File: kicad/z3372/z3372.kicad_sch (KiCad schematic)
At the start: 34 parts, among them J1 Conn_01x01, J2 Conn_01x02, J3 Conn_02x20_Odd_Even, Q4 MMBT3904, U1 MUX508, U15 M24C02-WMN, U2 MUX508, U3 TL074, U7 CAT9555YI-T2

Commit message: checkpoint z3372 v0.4
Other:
- sheet DAC ports: added FINAL_VCA4_CV; removed none
- sheet filter_as3372 ports: added VCA4_CV; removed none
- note added: "GPIO Module Driven: This mess is intended to be a peak voltage detector with a short hold cap. Trigger a +5V gate for the GPIO Module Driven signal. This can be used to crudely calibrate the noise level or resonance."
- note removed: "GPIO Module Driven: This mess is intended to be a peak voltage detector with a hold cap that doesn't hold all that long. Trigger a +5V gate for the GPIO Module Driven signal. This can be used to crudely calibrate the noise level or resonance."
- title: Z3372 Signal Processing -> Z3372 Signal Processor

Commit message: schematic done.  some values need tweaking.  design review still needed
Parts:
- removed unit 3 of U3
- added C29: 1u, Capacitor_SMD:C_0603_1608Metric, symbol Device:C
- added R35: 4k7, Resistor_SMD:R_1206_3216Metric, symbol Device:R
- added U5: LM4040AIM3-2.5, Package_TO_SOT_SMD:SOT-23, symbol Reference_Voltage:LM4040DBZ-2.5
- U1, U2: symbol as3372_lib:PS508-Analog_Switch -> z3372_lib:PS508-Analog_Switch
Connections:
- net +5V: now also R35.1
- net GND: now also C29.2, U5.2 (A)
- net PAN_FM_CTRL: now reaches U7.9 (IO0_5)
- net WHITE_NOISE_CTRL: no longer names the net of U7.10 (IO0_6)
- new net VREF_2.5V: C29.1, R35.2, U5.1 (K)
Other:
- sheet DAC ports: added MOD_AMOUNT_CV, VREF_2.5; removed MOD_AMOUNT_VCA3_CV
- sheet filter_as3372 ports: added PAN_FM_CTRL, VREF_2.5; removed NOISE_CTRL
- note added: "LM4040 resistor rough calc: Ilm4040 min: 70uA Vref input impedance: 3k8"
- note added: "TODO: this is likely ~3k"
- note removed: "Spares"
- moved on the sheet: C1, C2, C21, C3, C4, C5, C6, D1, Q4, R1, R17, R2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

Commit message: review underway for AS3372
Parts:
- removed C21: 0.1u, Capacitor_SMD:C_0603_1608Metric, symbol Device:C
- added unit 3 of U3
- R3: value 4k7 -> 100k; LCSC Part C23162 -> (none)
- R35: value 4k7 -> 3k; LCSC Part C17936 -> (none)
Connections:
- net GND: now also U3.10 (+)
- new net: U3.8, U3.9 (-)
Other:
- note added: "LM4040 resistor calc: Vref input impedance total: 3k8 ==> 657 uA lm4040 min: 80uA; with margin shoot for 150uA 657 + 150 ==> 807 uA through R. R = 3097. Use 3k which gives 833 uA."
- note added: "Spares"
- note added: "Voltage Reference"
- note removed: "LM4040 resistor rough calc: Ilm4040 min: 70uA Vref input impedance: 3k8"
- note removed: "TODO: this is likely ~3k"
- moved on the sheet: D4, R3

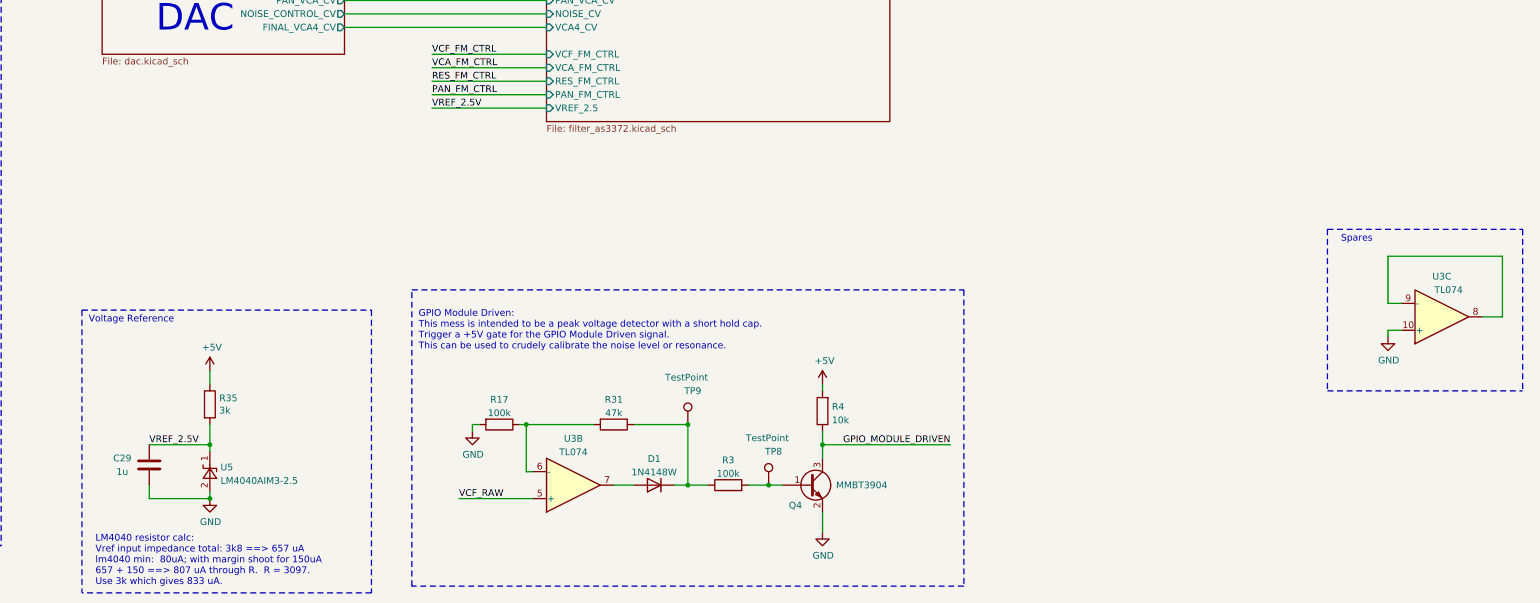
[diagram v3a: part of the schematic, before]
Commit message: schematic completed, working on place and route
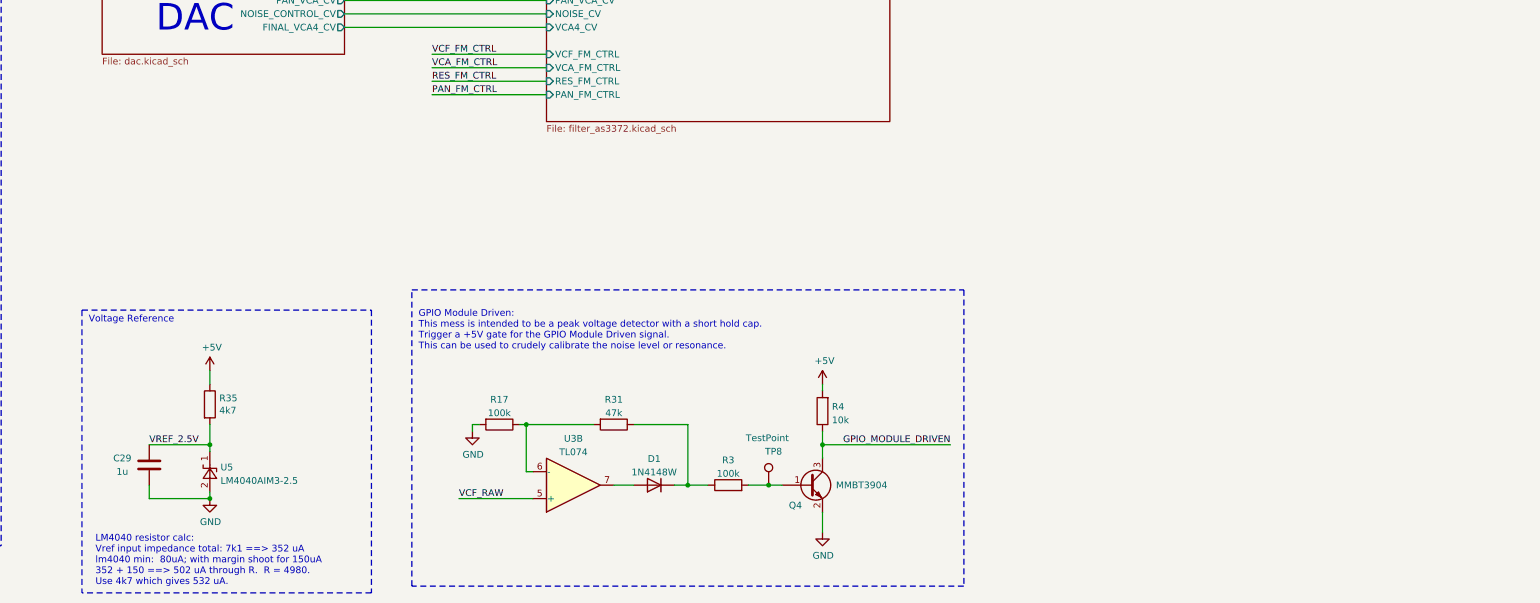
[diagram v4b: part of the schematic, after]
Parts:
- removed TP9: TestPoint, TestPoint:TestPoint_Pad_2.0x2.0mm, symbol Connector:TestPoint
- removed unit 3 of U3
- C29: footprint Capacitor_SMD:C_0603_1608Metric -> Capacitor_SMD:C_0805_2012Metric; LCSC Part (none) -> C28323
- R1, R2: footprint Resistor_SMD:R_0402_1005Metric -> Resistor_SMD:R_0603_1608Metric; LCSC Part C25741 -> C25803
- R3: LCSC Part (none) -> C25803
- R35: value 3k -> 4k7; footprint Resistor_SMD:R_1206_3216Metric -> Resistor_SMD:R_0603_1608Metric; LCSC Part (none) -> C23162
- U3: footprint Package_SO:SOIC-14_3.9x8.7mm_P1.27mm -> Package_SO:TSSOP-14_4.4x5mm_P0.65mm; LCSC Part C12594 -> C96507
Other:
- sheet filter_as3372 ports: added none; removed VREF_2.5
- note added: "LM4040 resistor calc: Vref input impedance total: 7k1 ==> 352 uA lm4040 min: 80uA; with margin shoot for 150uA 352 + 150 ==> 502 uA through R. R = 4980. Use 4k7 which gives 532 uA."
- note removed: "LM4040 resistor calc: Vref input impedance total: 3k8 ==> 657 uA lm4040 min: 80uA; with margin shoot for 150uA 657 + 150 ==> 807 uA through R. R = 3097. Use 3k which gives 833 uA."
- note removed: "Spares"

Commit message: placement improvements
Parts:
- added unit 2 of U3
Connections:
- net GND: now also U3.5 (+)
- net VCF_RAW: now also U3.3 (+); no longer U3.5 (+)
- net VCF_SIGNAL2: now also U3.8, U3.9 (-); no longer U3.1, U3.2 (-)
- net at R2.2, U2.8 (D): now also U3.10 (+); no longer U3.3 (+)
- net at R17.1, R31.2: now also U3.2 (-); no longer U3.6 (-)
- net at D1.2 (A): now also U3.1; no longer U3.7
- new net: U3.6 (-), U3.7
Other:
- note added: "Spares"

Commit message: continue routing
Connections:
- net LED_CTRL: now also U7.4 (IO0_0); no longer U7.6 (IO0_2)
- net RES_FM_CTRL: now also U7.7 (IO0_3); no longer U7.5 (IO0_1)
- net VCF_FM_CTRL: now also U7.6 (IO0_2); no longer U7.4 (IO0_0)
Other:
- moved on the sheet: D4, R56
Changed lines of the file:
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@@
   (no_connect (at 77.47 33.02))
   (no_connect (at 193.04 62.23))
-  (no_connect (at 193.04 52.07))
+  (no_connect (at 193.04 46.99))
   (no_connect (at 64.77 30.48))
   (wire (pts (xy 256.54 245.11) (xy 260.35 245.11))
@@
     (stroke (width 0) (type default))
   )
-  (wire (pts (xy 193.04 46.99) (xy 212.09 46.99))
+  (wire (pts (xy 193.04 52.07) (xy 212.09 52.07))
     (stroke (width 0) (type default))
   )
@@
     (stroke (width 0) (type default))
   )
-  (wire (pts (xy 222.25 46.99) (xy 222.25 49.53))
+  (wire (pts (xy 220.98 41.91) (xy 220.98 44.45))
     (stroke (width 0) (type default))
   )
@@
     (stroke (width 0) (type dash))
   )
-  (wire (pts (xy 193.04 49.53) (xy 214.63 49.53))
-    (stroke (width 0) (type default))
-  )
   (wire (pts (xy 93.98 138.43) (xy 96.52 138.43))
     (stroke (width 0) (type default))
   )
-  (wire (pts (xy 222.25 36.83) (xy 222.25 39.37))
+  (wire (pts (xy 220.98 31.75) (xy 220.98 34.29))
     (stroke (width 0) (type default))
   )
@@
     (stroke (width 0) (type dash))
   )
+  (wire (pts (xy 193.04 54.61) (xy 212.09 54.61))
+    (stroke (width 0) (type default))
+  )
   (wire (pts (xy 104.14 55.88) (xy 104.14 60.96))
     (stroke (width 0) (type default))
@@
     (stroke (width 0) (type default))
   )
-  (wire (pts (xy 193.04 54.61) (xy 212.09 54.61))
-    (stroke (width 0) (type default))
-  )
   (wire (pts (xy 110.49 245.11) (xy 107.95 245.11))
     (stroke (width 0) (type default))
@@
     (stroke (width 0) (type default))
   )
+  (wire (pts (xy 193.04 44.45) (xy 213.36 44.45))
+    (stroke (width 0) (type default))
+  )
   (wire (pts (xy 403.86 208.28) (xy 405.13 208.28))
     (stroke (width 0) (type default))
@@
     (stroke (width 0) (type default))
   )
-  (wire (pts (xy 193.04 44.45) (xy 212.09 44.45))
+  (wire (pts (xy 193.04 49.53) (xy 212.09 49.53))
     (stroke (width 0) (type default))
   )
@@
     (effects (font (size 1.27 1.27)) (justify right bottom))
   )
-  (label "LED_CTRL" (at 199.39 49.53 0) (fields_autoplaced)
-    (effects (font (size 1.27 1.27)) (justify left bottom))
+  (label "LED_CTRL" (at 212.09 44.45 180) (fields_autoplaced)
+    (effects (font (size 1.27 1.27)) (justify right bottom))
   )
   (label "VCF_SIG2_CTRL0" (at 45.72 240.03 270) (fields_autoplaced)
@@
     (effects (font (size 1.27 1.27)) (justify left bottom))
   )
-  (label "RES_FM_CTRL" (at 212.09 46.99 180) (fields_autoplaced)
+  (label "RES_FM_CTRL" (at 212.09 52.07 180) (fields_autoplaced)
     (effects (font (size 1.27 1.27)) (justify right bottom))
   )
@@
     (effects (font (size 1.27 1.27)) (justify left bottom))
   )
-  (label "VCF_FM_CTRL" (at 212.09 44.45 180) (fields_autoplaced)
+  (label "VCF_FM_CTRL" (at 212.09 49.53 180) (fields_autoplaced)
     (effects (font (size 1.27 1.27)) (justify right bottom))
   )
@@
     )
   )
-  (symbol (lib_id "Device:R") (at 222.25 43.18 0) (unit 1)
-    (in_bom yes) (on_board yes) (dnp no)
-    (property "Reference" "R56" (at 227.5078 43.18 90)
-      (effects (font (size 1.27 1.27)))
-    )
-    (property "Value" "2k" (at 225.1964 43.18 90)
-      (effects (font (size 1.27 1.27)))
-    )
-    (property "Footprint" "Resistor_SMD:R_0603_1608Metric" (at 220.472 43.18 90)
-      (effects (font (size 1.27 1.27)) hide)
-    )
-    (property "Datasheet" "~" (at 222.25 43.18 0)
-      (effects (font (size 1.27 1.27)) hide)
-    )
-    (property "LCSC Part" "C22975" (at 222.25 43.18 0)
+  (symbol (lib_id "Device:R") (at 220.98 38.1 0) (unit 1)
+    (in_bom yes) (on_board yes) (dnp no)
+    (property "Reference" "R56" (at 226.2378 38.1 90)
+      (effects (font (size 1.27 1.27)))
+    )
+    (property "Value" "2k" (at 223.9264 38.1 90)
+      (effects (font (size 1.27 1.27)))
+    )
+    (property "Footprint" "Resistor_SMD:R_0603_1608Metric" (at 219.202 38.1 90)
+      (effects (font (size 1.27 1.27)) hide)
+    )
+    (property "Datasheet" "~" (at 220.98 38.1 0)
+      (effects (font (size 1.27 1.27)) hide)
+    )
+    (property "LCSC Part" "C22975" (at 220.98 38.1 0)
       (effects (font (size 1.27 1.27)) hide)
     )
@@
     )
   )
-  (symbol (lib_id "Device:LED") (at 218.44 49.53 0) (mirror x) (unit 1)
-    (in_bom yes) (on_board yes) (dnp no)
-    (property "Reference" "D4" (at 218.2622 55.0418 0)
-      (effects (font (size 1.27 1.27)))
-    )
-    (property "Value" "LED" (at 218.2622 52.7304 0)
-      (effects (font (size 1.27 1.27)))
-    )
-    (property "Footprint" "LED_SMD:LED_0603_1608Metric" (at 218.44 49.53 0)
-      (effects (font (size 1.27 1.27)) hide)
-    )
-    (property "Datasheet" "~" (at 218.44 49.53 0)
-      (effects (font (size 1.27 1.27)) hide)
-    )
-    (property "LCSC Part" "C2286" (at 218.44 49.53 0)
+  (symbol (lib_id "Device:LED") (at 217.17 44.45 0) (mirror x) (unit 1)
+    (in_bom yes) (on_board yes) (dnp no)
+    (property "Reference" "D4" (at 216.9922 49.9618 0)
+      (effects (font (size 1.27 1.27)))
+    )
+    (property "Value" "LED" (at 216.9922 47.6504 0)
+      (effects (font (size 1.27 1.27)))
+    )
+    (property "Footprint" "LED_SMD:LED_0603_1608Metric" (at 217.17 44.45 0)
+      (effects (font (size 1.27 1.27)) hide)
+    )
+    (property "Datasheet" "~" (at 217.17 44.45 0)
+      (effects (font (size 1.27 1.27)) hide)
+    )
+    (property "LCSC Part" "C2286" (at 217.17 44.45 0)
       (effects (font (size 1.27 1.27)) hide)
     )
@@
     )
   )
-  (symbol (lib_id "power:+5V") (at 222.25 36.83 0) (unit 1)
-    (in_bom yes) (on_board yes) (dnp no)
-    (property "Reference" "#PWR0112" (at 222.25 40.64 0)
-      (effects (font (size 1.27 1.27)) hide)
-    )
-    (property "Value" "+5V" (at 222.631 32.4358 0)
-      (effects (font (size 1.27 1.27)))
-    )
-    (property "Footprint" "" (at 222.25 36.83 0)
-      (effects (font (size 1.27 1.27)) hide)
-    )
-    (property "Datasheet" "" (at 222.25 36.83 0)
-      (effects (font (size 1.27 1.27)) hide)
-    )
+  (symbol (lib_id "power:+5V") (at 220.98 31.75 0) (unit 1)
+    (in_bom yes) (on_board yes) (dnp no)
+    (property "Reference" "#PWR0112" (at 220.98 35.56 0)
+      (effects (font (size 1.27 1.27)) hide)
+    )
+    (property "Value" "+5V" (at 221.361 27.3558 0)
+      (effects (font (size 1.27 1.27)))
+    )
+    (property "Footprint" "" (at 220.98 31.75 0)
+      (effects (font (size 1.27 1.27)) hide)
+    )
+    (property "Datasheet" "" (at 220.98 31.75 0)
+      (effects (font (size 1.27 1.27)) hide)
+    )

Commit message: getting some cleanup done
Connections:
- net GND: no longer C29.2
- net VREF_2.5V: no longer C29.1
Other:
- moved on the sheet: C29, U5
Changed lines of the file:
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@@
     )
   )
-  (symbol (lib_id "Device:R") (at 166.37 229.87 0) (unit 1)
-    (in_bom yes) (on_board yes) (dnp no)
-    (property "Reference" "R35" (at 168.148 228.7016 0)
-      (effects (font (size 1.27 1.27)) (justify left))
-    )
-    (property "Value" "4k7" (at 168.148 231.013 0)
-      (effects (font (size 1.27 1.27)) (justify left))
-    )
-    (property "Footprint" "Resistor_SMD:R_0603_1608Metric" (at 164.592 229.87 90)
+  (symbol (lib_id "Device:R") (at 166.37 229.87 0) (mirror y) (unit 1)
+    (in_bom yes) (on_board yes) (dnp no)
+    (property "Reference" "R35" (at 164.592 228.7016 0)
+      (effects (font (size 1.27 1.27)) (justify left))
+    )
+    (property "Value" "4k7" (at 164.592 231.013 0)
+      (effects (font (size 1.27 1.27)) (justify left))
+    )
+    (property "Footprint" "Resistor_SMD:R_0603_1608Metric" (at 168.148 229.87 90)
       (effects (font (size 1.27 1.27)) hide)
     )
@@
     )
   )
-  (symbol (lib_id "Device:C") (at 154.94 241.3 0) (unit 1)
-    (in_bom yes) (on_board yes) (dnp no)
-    (property "Reference" "C29" (at 149.86 240.03 0)
-      (effects (font (size 1.27 1.27)))
-    )
-    (property "Value" "1u" (at 149.86 242.57 0)
-      (effects (font (size 1.27 1.27)))
-    )
-    (property "Footprint" "Capacitor_SMD:C_0805_2012Metric" (at 155.9052 245.11 0)
-      (effects (font (size 1.27 1.27)) hide)
-    )
-    (property "Datasheet" "~" (at 154.94 241.3 0)
-      (effects (font (size 1.27 1.27)) hide)
-    )
-    (property "LCSC Part" "C28323" (at 154.94 241.3 0)
+  (symbol (lib_id "Device:C") (at 177.8 241.3 0) (mirror y) (unit 1)
+    (in_bom yes) (on_board yes) (dnp no)
+    (property "Reference" "C29" (at 182.88 240.03 0)
+      (effects (font (size 1.27 1.27)))
+    )
+    (property "Value" "1u" (at 182.88 242.57 0)
+      (effects (font (size 1.27 1.27)))
+    )
+    (property "Footprint" "Capacitor_SMD:C_0805_2012Metric" (at 176.8348 245.11 0)
+      (effects (font (size 1.27 1.27)) hide)
+    )
+    (property "Datasheet" "~" (at 177.8 241.3 0)
+      (effects (font (size 1.27 1.27)) hide)
+    )
+    (property "LCSC Part" "C28323" (at 177.8 241.3 0)
       (effects (font (size 1.27 1.27)) hide)
     )
@@
     )
   )
-  (symbol (lib_id "Reference_Voltage:LM4040DBZ-2.5") (at 166.37 242.57 90) (unit 1)
+  (symbol (lib_id "Reference_Voltage:LM4040DBZ-2.5") (at 166.37 242.57 270) (mirror x) (unit 1)
     (in_bom yes) (on_board yes) (dnp no) (fields_autoplaced)
-    (property "Reference" "U5" (at 168.3766 241.7353 90)
+    (property "Reference" "U5" (at 164.3634 241.7353 90)
       (effects (font (size 1.27 1.27)) (justify right))
     )
-    (property "Value" "LM4040AIM3-2.5" (at 168.3766 244.2722 90)
+    (property "Value" "LM4040AIM3-2.5" (at 164.3634 244.2722 90)
       (effects (font (size 1.27 1.27)) (justify right))
     )
-    (property "Footprint" "Package_TO_SOT_SMD:SOT-23" (at 171.45 242.57 0)
+    (property "Footprint" "Package_TO_SOT_SMD:SOT-23" (at 161.29 242.57 0)
       (effects (font (size 1.27 1.27) italic) hide)
     )

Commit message: silk front better
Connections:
- net GND: now also C29.2
- net VREF_2.5V: now also C29.1
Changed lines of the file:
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@@
+    (stroke (width 0) (type default))
+  )
+  (wire (pts (xy 166.37 237.49) (xy 177.8 237.49))
     (stroke (width 0) (type default))
   )
@@
     (stroke (width 0) (type default))
   )
-  (wire (pts (xy 154.94 247.65) (xy 166.37 247.65))
-    (stroke (width 0) (type default))
-  )
   (wire (pts (xy 68.58 243.84) (xy 68.58 240.03))
     (stroke (width 0) (type default))
@@
     (stroke (width 0) (type dash))
   )
-  (wire (pts (xy 154.94 245.11) (xy 154.94 247.65))
-    (stroke (width 0) (type default))
-  )
   (wire (pts (xy 256.54 233.68) (xy 256.54 245.11))
     (stroke (width 0) (type default))
@@
     (stroke (width 0) (type default))
   )
+  (wire (pts (xy 177.8 247.65) (xy 166.37 247.65))
+    (stroke (width 0) (type default))
+  )
   (wire (pts (xy 77.47 71.12) (xy 104.14 71.12))
     (stroke (width 0) (type default))
@@
     (stroke (width 0) (type default))
   )
-  (wire (pts (xy 154.94 237.49) (xy 166.37 237.49))
-    (stroke (width 0) (type default))
-  )
   (wire (pts (xy 107.95 241.3) (xy 107.95 245.11))
     (stroke (width 0) (type default))
@@
   )
   (wire (pts (xy 68.58 210.82) (xy 68.58 209.55))
+    (stroke (width 0) (type default))
+  )
+  (wire (pts (xy 177.8 245.11) (xy 177.8 247.65))
     (stroke (width 0) (type default))
   )
@@
     (effects (font (size 1.27 1.27)) (justify left bottom))
   )
-  (label "VREF_2.5V" (at 154.94 237.49 0) (fields_autoplaced)
-    (effects (font (size 1.27 1.27)) (justify left bottom))
+  (label "VREF_2.5V" (at 177.8 237.49 180) (fields_autoplaced)
+    (effects (font (size 1.27 1.27)) (justify right bottom))
   )
   (label "CARD3_OUT1" (at 92.71 58.42 180) (fields_autoplaced)
